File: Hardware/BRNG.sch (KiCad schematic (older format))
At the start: 81 parts, among them J1 ISP, J2 MOLEX 105017 0001, J3 CONNETTORE 6 PIN 90°, Q1 BC847, Q2 BC847, Q3 MMBTA42, Q4 BC847, Q5 BC847, SW1 DIPTRONICS NDI-02H-V, U1 LM555N, U2 ATMEGA328P-AU, U3 LM555N, U4 CH340G, Y1 16MHz LF XTAL003237, Y2 12MHz LF XTAL003210

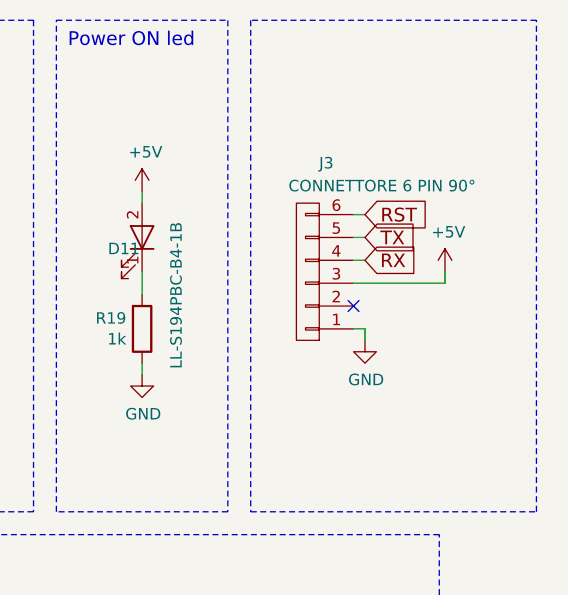
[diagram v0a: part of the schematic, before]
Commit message: Fixes #4
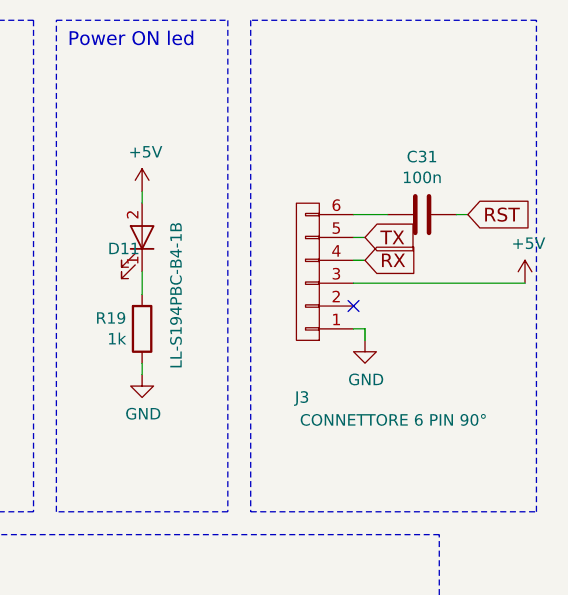
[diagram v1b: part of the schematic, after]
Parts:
- added C31: 100n, Capacitors_SMD:C_0805_HandSoldering, symbol C
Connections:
- net RST: now also C31.2; no longer J3.6 (P6)
- new net: C31.1, J3.6 (P6)
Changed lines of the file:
@@
 U 1 1 5A9C2EE1
 P 9100 1650
-F 0 "J3" H 9019 1175 50  0000 C CNN
-F 1 "CONNETTORE 6 PIN 90°" H 8775 1275 50  0000 C CNN
+F 0 "J3" H 9125 2200 50  0000 C CNN
+F 1 "CONNETTORE 6 PIN 90°" H 8725 2300 50  0000 C CNN
 F 2 "Pin_Headers:Pin_Header_Angled_1x06_Pitch2.54mm" H 9100 1650 50  0001 C CNN
 F 3 "" H 9100 1650 50  0001 C CNN
@@
 L +5V #PWR037
 U 1 1 5A9C342D
-P 9700 1650
-F 0 "#PWR037" H 9700 1500 50  0001 C CNN
-F 1 "+5V" H 9715 1823 50  0000 C CNN
-F 2 "" H 9700 1650 50  0001 C CNN
-F 3 "" H 9700 1650 50  0001 C CNN
-	1    9700 1650
+P 10050 1700
+F 0 "#PWR037" H 10050 1550 50  0001 C CNN
+F 1 "+5V" H 10065 1873 50  0000 C CNN
+F 2 "" H 10050 1700 50  0001 C CNN
+F 3 "" H 10050 1700 50  0001 C CNN
+	1    10050 1700
 	1    0    0    -1
 $EndComp
@@
 Text GLabel 9350 1500 2    60   Input ~ 0
 TX
-Text GLabel 9350 1400 2    60   Input ~ 0
+Text GLabel 9800 1400 2    60   Input ~ 0
 RST
 $Comp
@@
 $EndComp
 $Comp
-L +5V #PWR?
+L +5V #PWR047
 U 1 1 5A9EAAD6
 P 700 3125
-F 0 "#PWR?" H 700 2975 50  0001 C CNN
+F 0 "#PWR047" H 700 2975 50  0001 C CNN
 F 1 "+5V" H 775 2950 50  0000 C CNN
 F 2 "" H 700 3125 50  0001 C CNN
@@
 	9350 1900 9300 1900
 Wire Wire Line
-	9700 1650 9700 1700
-Wire Wire Line
-	9700 1700 9300 1700
-Wire Wire Line
-	9350 1400 9300 1400
+	9300 1700 10050 1700
+Wire Wire Line
+	9300 1400 9450 1400
 Wire Wire Line
 	9350 1500 9300 1500
@@
 	1    0    0    -1
 $EndComp
+$Comp
+L C C31
+U 1 1 5AEBBDEE
+P 9600 1400
+F 0 "C31" V 9852 1400 50  0000 C CNN
+F 1 "100n" V 9761 1400 50  0000 C CNN
+F 2 "Capacitors_SMD:C_0805_HandSoldering" H 9638 1250 50  0001 C CNN
+F 3 "" H 9600 1400 50  0001 C CNN
+	1    9600 1400
+	0    -1   -1   0
+$EndComp
+Wire Wire Line
+	9750 1400 9800 1400
 $EndSCHEMATC
